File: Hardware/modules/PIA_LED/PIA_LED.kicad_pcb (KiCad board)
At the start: 4 copper layers, 83.3 x 68.2 mm, 42 parts, among them J1 Bus_PCI_6502, J2 PIA_A, J3 PIA_B, U1 6520, U2 74HC138

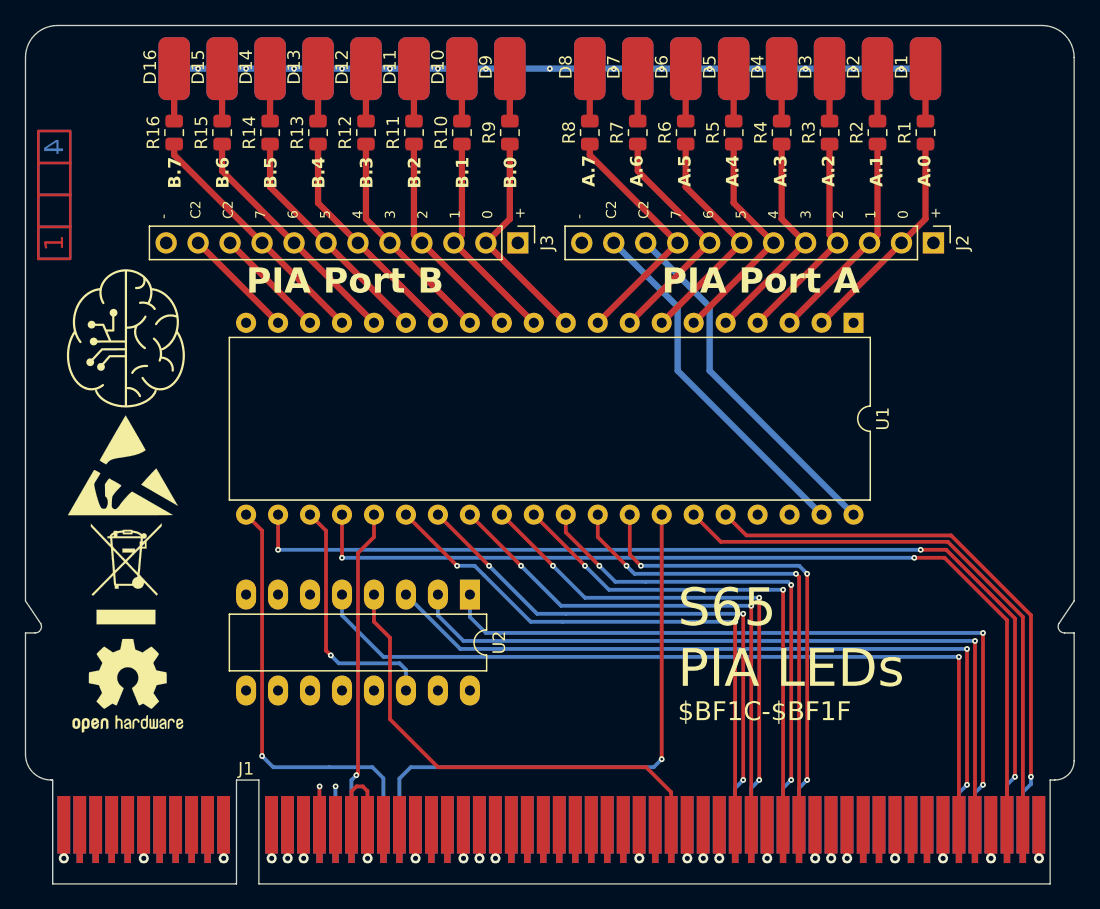
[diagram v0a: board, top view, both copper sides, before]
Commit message: Hardware Update Add MyCPU VGA Module Beautify all Schematics minor Error corrections Readme Update
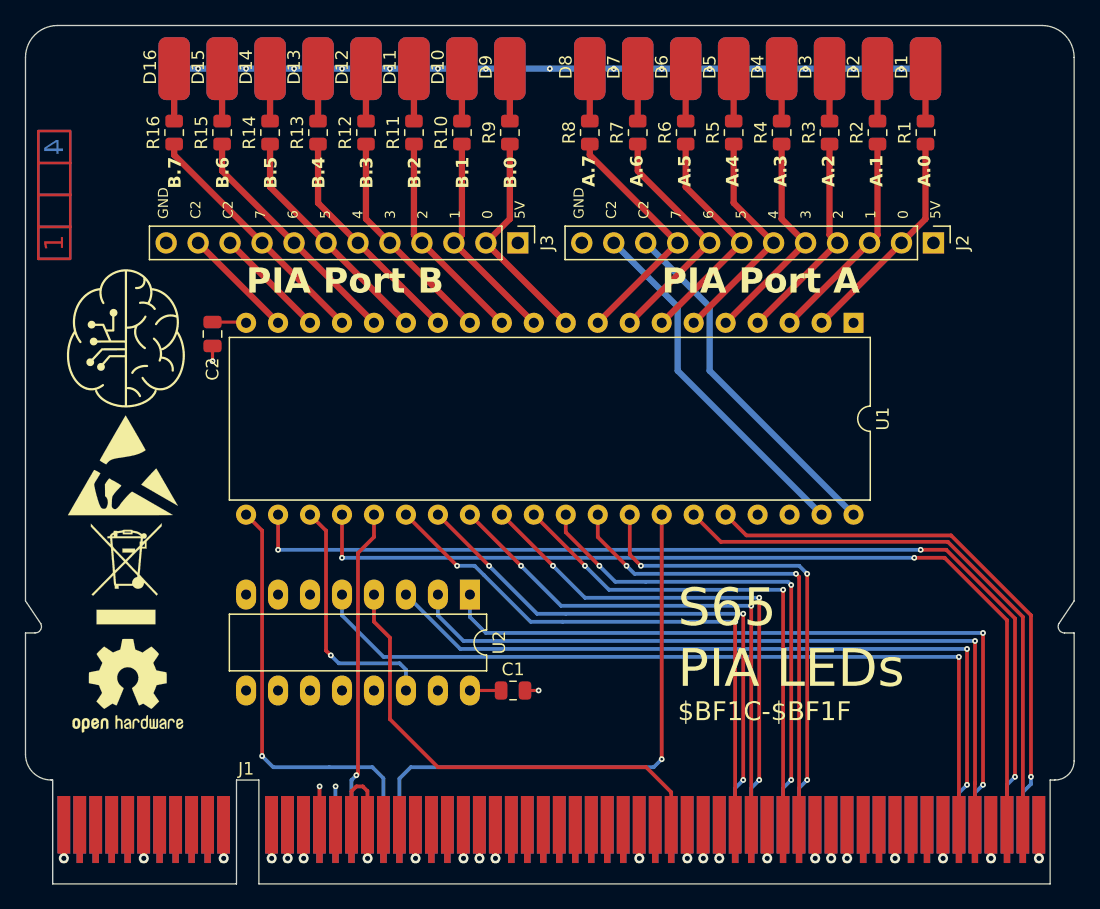
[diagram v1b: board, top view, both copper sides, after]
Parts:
- added C1: 100n, Capacitor_SMD:C_0805_2012Metric, F.Cu at (163.4, 86.4)
- added C2: 100n, Capacitor_SMD:C_0805_2012Metric, F.Cu at (139.6, 58.0)
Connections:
- J1 pad A11: /A13 -> unconnected-(J1-A13-PadA11)_0
- J1 pad A12: /A15 -> unconnected-(J1-A15-PadA12)
- J1 pad A25: /~{ROM} -> unconnected-(J1-~{ROM}-PadA25)
- J1 pad A27: /~{IRQ_0.0} -> unconnected-(J1-~{IRQ_0.0}-PadA27)
- J1 pad A28: /~{IRQ_0.1} -> unconnected-(J1-~{IRQ_0.1}-PadA28)
- J1 pad A29: /~{IRQ_0.2} -> unconnected-(J1-~{IRQ_0.2}-PadA29)_0
- J1 pad A30: /~{IRQ_0.3} -> unconnected-(J1-~{IRQ_0.3}-PadA30)
- J1 pad A31: /~{IRQ_0.4} -> unconnected-(J1-~{IRQ_0.4}-PadA31)_0
- J1 pad A32: /~{IRQ_0.5} -> unconnected-(J1-~{IRQ_0.5}-PadA32)
- J1 pad A33: /~{IRQ_0.6} -> unconnected-(J1-~{IRQ_0.6}-PadA33)_0
- J1 pad A34: /~{IRQ_0.7} -> unconnected-(J1-~{IRQ_0.7}-PadA34)
- J1 pad A38: /SYNC_VPA -> unconnected-(J1-Sync/VPA-PadA38)_0
- J1 pad A39: /Ø2/VDA -> unconnected-(J1-Ø2/VDA-PadA39)_0
- J1 pad A41: /~{RDY} -> unconnected-(J1-~{RDY}-PadA41)
- J1 pad A42: /~{BE} -> unconnected-(J1-~{BE}-PadA42)
- J1 pad A45: /E -> unconnected-(J1-E-PadA45)_0
- J1 pad A53: /RAM_0 -> unconnected-(J1-RAM0-PadA53)_0
- J1 pad A54: /RAM_1 -> unconnected-(J1-RAM1-PadA54)
- J1 pad A55: /RAM_2 -> unconnected-(J1-RAM2-PadA55)
- J1 pad A56: /RAM_3 -> unconnected-(J1-RAM3-PadA56)
- J1 pad A58: /RAM_4 -> unconnected-(J1-RAM4-PadA58)_0
- J1 pad A59: /RAM_5 -> unconnected-(J1-RAM5-PadA59)
- J1 pad A60: /RAM_6 -> unconnected-(J1-RAM6-PadA60)_0
- J1 pad A61: /RAM_7 -> unconnected-(J1-RAM7-PadA61)_0
- J1 pad A8: /A9 -> unconnected-(J1-A9-PadA8)_0
- J1 pad A9: /A11 -> unconnected-(J1-A11-PadA9)_0
- J1 pad B11: /A12 -> unconnected-(J1-A12-PadB11)
- J1 pad B12: /A14 -> unconnected-(J1-A14-PadB12)_0
- J1 pad B24: /~{L_RAM} -> unconnected-(J1-~{L_RAM}-PadB24)_0
- J1 pad B25: /~{H_RAM} -> unconnected-(J1-~{H_RAM}-PadB25)_0
- J1 pad B27: /~{IRQ} -> unconnected-(J1-~{IRQ}-PadB27)_0
- J1 pad B28: /~{IRQ_0} -> unconnected-(J1-~{IRQ_0}-PadB28)
- J1 pad B29: /~{IRQ_1} -> unconnected-(J1-~{IRQ_1}-PadB29)_0
- J1 pad B30: /~{IRQ_2} -> unconnected-(J1-~{IRQ_2}-PadB30)
- J1 pad B31: /~{IRQ_3} -> unconnected-(J1-~{IRQ_3}-PadB31)_0
- J1 pad B32: /~{IRQ_4} -> unconnected-(J1-~{IRQ_4}-PadB32)
- J1 pad B33: /~{NMI} -> unconnected-(J1-~{NMI}-PadB33)_0
- J1 pad B34: /PAGE -> unconnected-(J1-PAGE_ROM-PadB34)_0
- J1 pad B38: /~{VP} -> unconnected-(J1-~{VP}-PadB38)
- J1 pad B39: /~{ML} -> unconnected-(J1-~{ML}-PadB39)_0
- J1 pad B46: /M/X -> unconnected-(J1-M/~{X}-PadB46)
- J1 pad B53: /ROM_0 -> unconnected-(J1-ROM0-PadB53)_0
- J1 pad B54: /ROM_1 -> unconnected-(J1-ROM1-PadB54)
- J1 pad B55: /ROM_2 -> unconnected-(J1-ROM2-PadB55)
- J1 pad B56: /ROM_3 -> unconnected-(J1-ROM3-PadB56)
- J1 pad B58: /ROM_4 -> unconnected-(J1-ROM4-PadB58)_0
- J1 pad B59: /ROM_5 -> unconnected-(J1-ROM5-PadB59)_0
- J1 pad B60: /ROM_6 -> unconnected-(J1-ROM6-PadB60)
- J1 pad B61: /ROM_7 -> unconnected-(J1-ROM7-PadB61)_0
- J1 pad B8: /A8 -> unconnected-(J1-A8-PadB8)_0
- J1 pad B9: /A10 -> unconnected-(J1-A10-PadB9)
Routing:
- net +5V: track 0.00 -> 5.17 mm
- net GND: track 72.7 -> 75.0 mm, vias 35 -> 37
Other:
- board text added: "GND C2 C2 7 6 5 4 3 2 1 0 5V"
- board text removed: "- C2 C2 7 6 5 4 3 2 1 0 +"

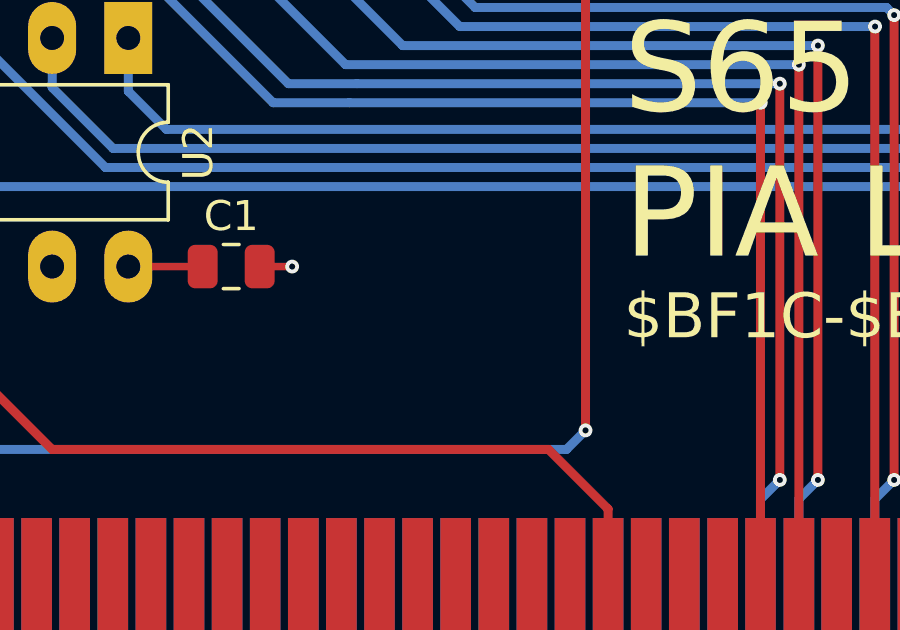
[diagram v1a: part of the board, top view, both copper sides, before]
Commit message: Hardware Review Pt. 1 fix Address Decoding for Strobe Generators add bulk capacitance to every board fix wiring of Prototyping Board
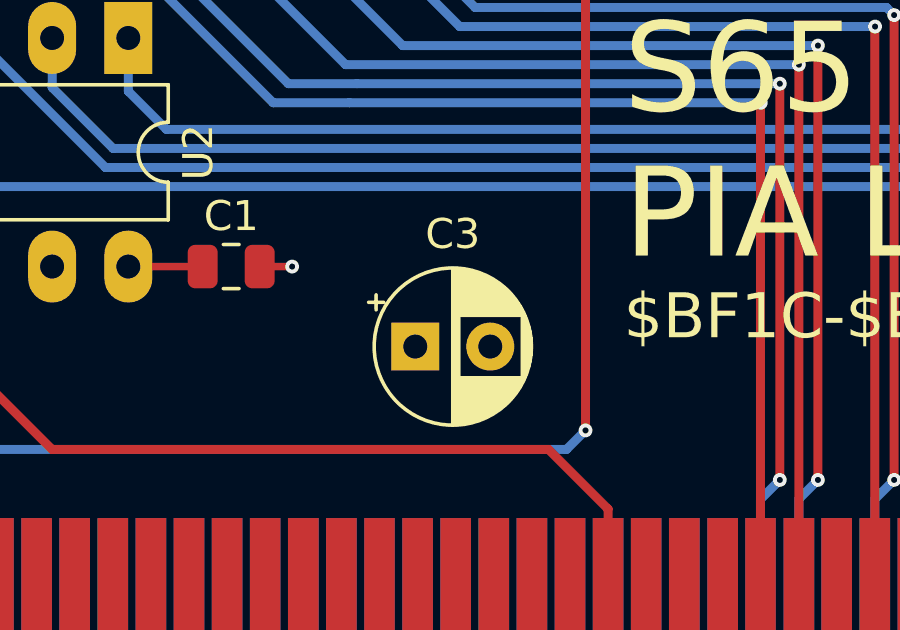
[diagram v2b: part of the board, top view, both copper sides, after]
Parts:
- added C3: 10µ, Capacitor_THT:CP_Radial_D5.0mm_P2.50mm, F.Cu at (169.6, 89.0)

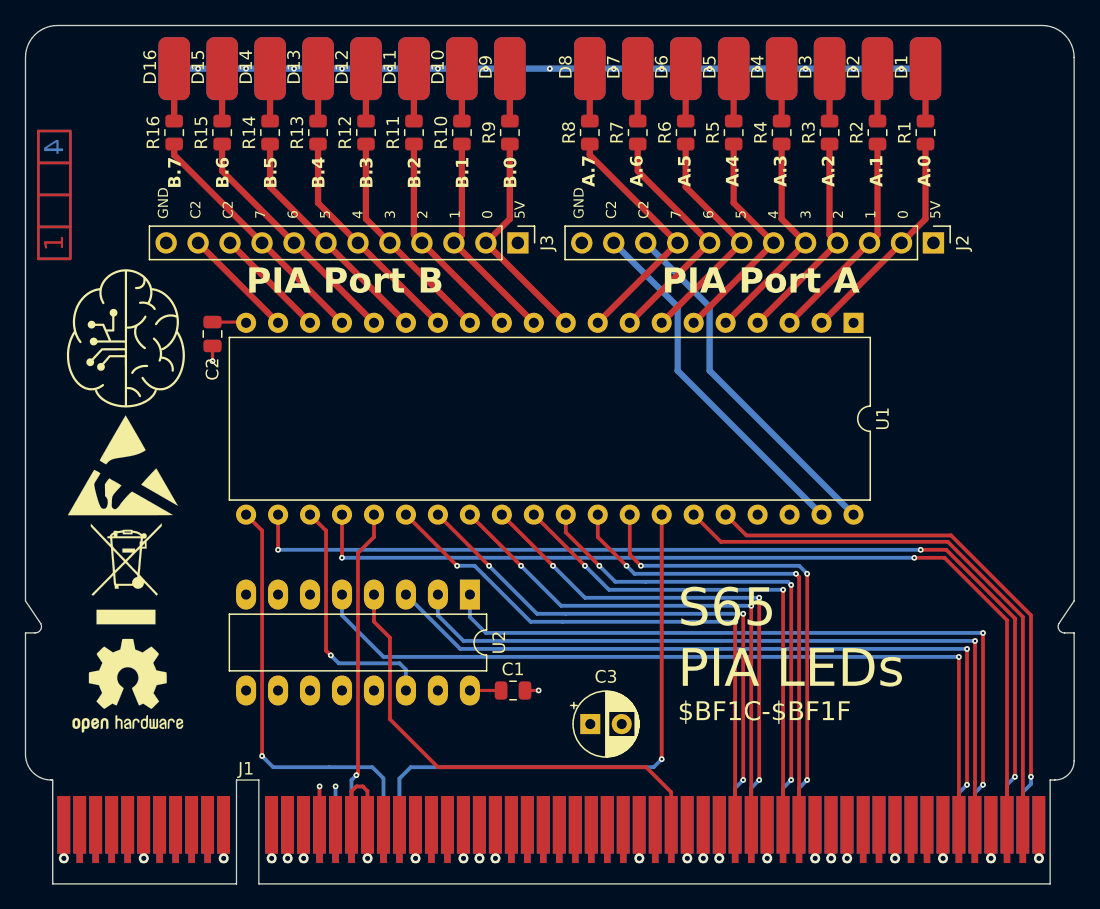
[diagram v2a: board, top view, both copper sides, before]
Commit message: Big Review Update - Changed Copper Pours on all PCBs - Implemented errors found at review - fixed some additional errors
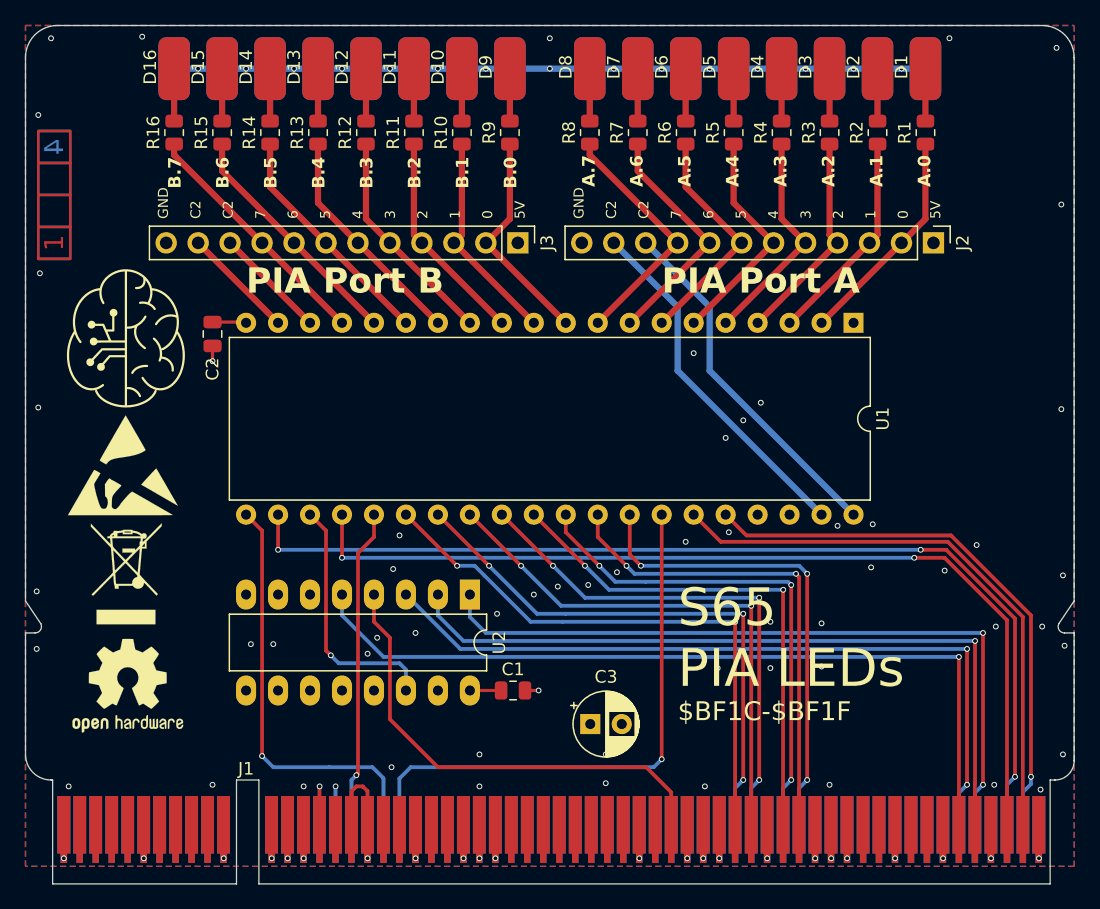
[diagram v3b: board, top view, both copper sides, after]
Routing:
- net +5V: vias 4 -> 61
- added copper zone on B.Cu, net +5V
- added copper zone on F.Cu, net +5V
- added copper zone on In1.Cu, net GND
- removed copper zone on In1.Cu, net +5V
